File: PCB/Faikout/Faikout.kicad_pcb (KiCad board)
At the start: 2 copper layers, 70 x 70 mm, 47 parts, among them J1 1x5, J2 TC2030-USB-NL, J3 Reset, Q1 BSS138PS, U1 TPS562246, U4 ESP32-S3-MINI-1-N4R2

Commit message: Silkscreen tidy
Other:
- board text removed: "3"

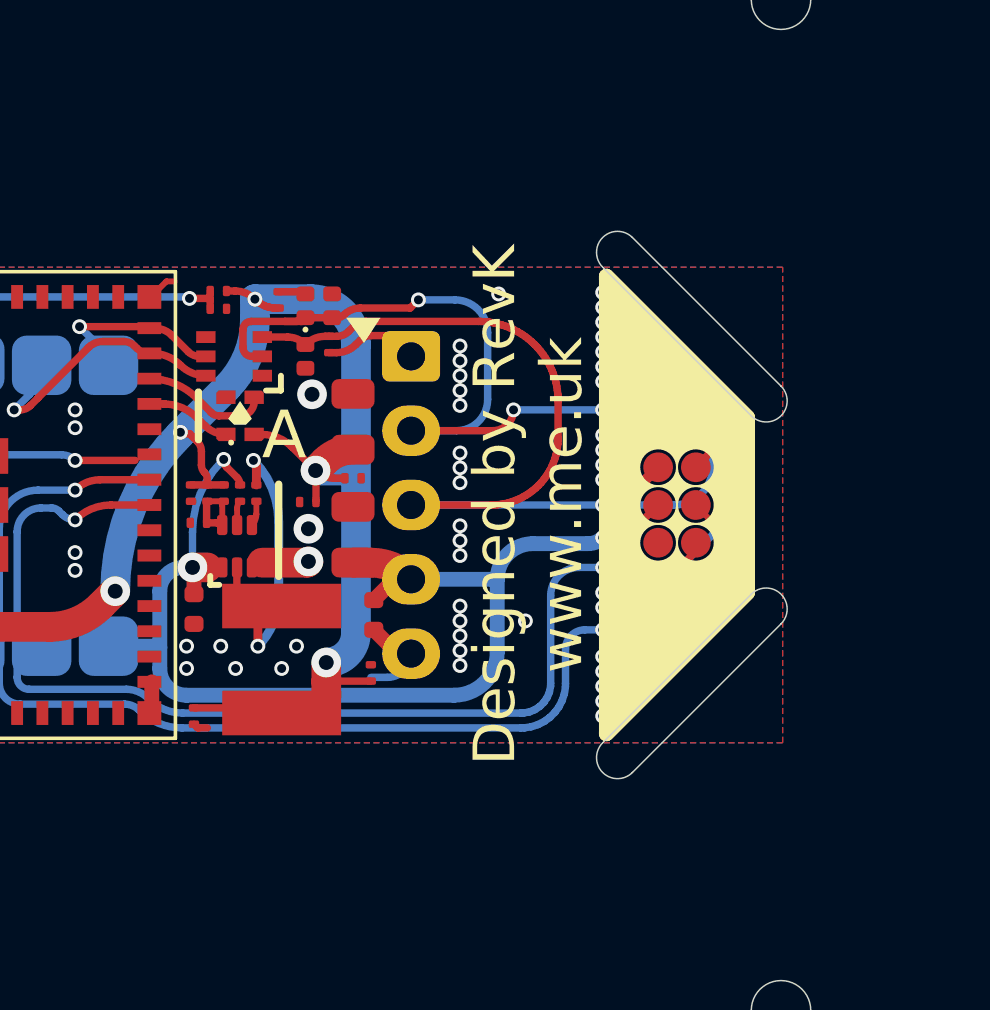
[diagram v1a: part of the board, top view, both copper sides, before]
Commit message: Remove logos & update the PCB to use 1x6 header instead of TC2030
Transitioned the programming interface to a more standard pin header and removed branding elements to make the project more open-source friendly.
* Programming Header (J2):
    * Replaced the TC2030 (Tag-Connect) interface with a standard 1x06 2.54mm vertical pin header.
    * Updated the footprint to Connector_PinHeader_2.54mm:PinHeader_1x06_P2.54mm_Vertical.
    * Updated schematic symbols and adjusted routing for the new header pinout (D+, D-, DC, and GND).
    * Updated schematic annotations to refer to "programming cable" instead of "TC2030m".
* Logo & Branding Removal:
    * Deleted "Andrews & Arnold Ltd" branding and AJK logos from the silkscreen.
    * Removed text elements referencing the original manufacturer (e.g., "Designed by RevK", "Made in China for...").
    * Updated project metadata (company name) to "Open Source".
* Misc Improvements:
    * Reoriented global labels and power symbols for better schematic readability.
    * Synchronized KiCad project files and updated footprint cache.
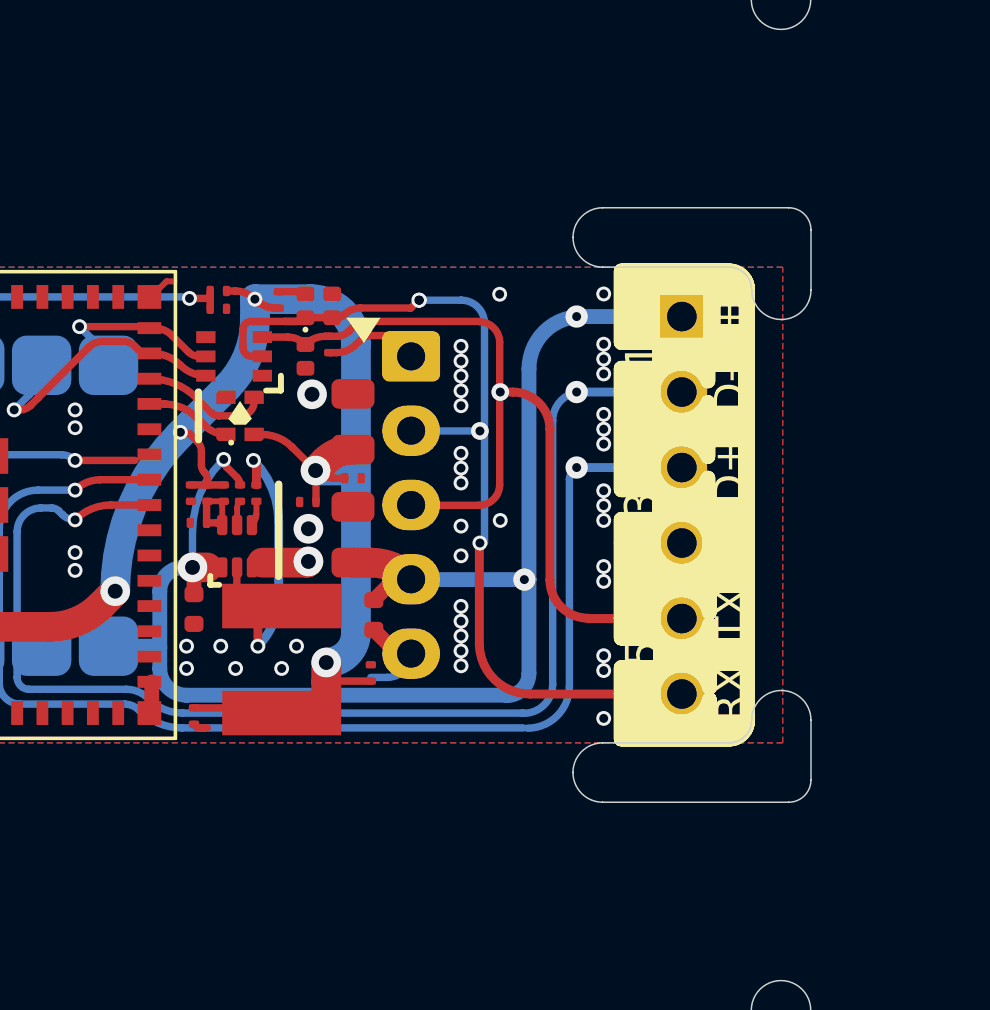
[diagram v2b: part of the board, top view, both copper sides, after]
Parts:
- J2: value TC2030-USB-NL -> PinHeader_2.54mm; footprint RevK:Tag-Connect_TC2030-IDC-NL_2x03_P1.27mm_Vertical -> Connector_PinHeader_2.54mm:PinHeader_1x06_P2.54mm_Vertical
- moved J2 0.17 mm to (154.7, 65.0), turned to 0 degrees
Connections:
- J2 pad 2: Net-(J1-Pin_3) -> D-
- J2 pad 3: D- -> D+
- J2 pad 4: D+ -> GND
- J2 pad 5: GND -> Net-(J1-Pin_3)
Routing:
- net DC: track 40.6 -> 48.9 mm, vias 3 -> 4
- net D-: track 37.1 -> 42.9 mm
- net Net-(D4-K): track 34.6 -> 31.4 mm
- net Net-(J1-Pin_3): track 32.1 -> 29.3 mm, vias 2 -> 1
- net D+: track 41.9 -> 42.5 mm
- net GND: vias 72 -> 68
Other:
- board text added: "3"
- board text removed: "A"
- board text removed: "Designed by RevK www.me.uk"
- board text removed: "E"
- board text removed: "Made in China for Andrews & Arnold Ltd"
- board text removed: "U"
- board text removed: "aikout.uk"
- board text removed: "www.f"
